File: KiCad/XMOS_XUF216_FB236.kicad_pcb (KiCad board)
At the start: 4 copper layers, 100 x 100 mm, 219 parts, among them J1 RJ45_Shielded, J10 Conn_02x10_FEMALE_toNext, J11 Conn_01x04, J12 Conn_01x08, J13 RJ45_Shielded, J14 RJ45_Shielded, J15 Conn_02x08_Odd_Even, J16 RJ45_Shielded, J17 RJ45_Shielded, J18 RJ45_Shielded, J19 RJ45_Shielded, J2 Barrel_Jack_MountingPin, J3 Conn_01x04, J4 RJ45_Shielded, J5 USB_B_Mini, J6 Conn_02x08_Odd_Even, J7 Mini-DIN-8, J8 Conn_02x10_MALE_FROM_XTAG, J9 Mini-DIN-8, M1 RFM-0505S, SW1 RESET, SW2 BOOT, SW3 GP, U1 DS90LV049TMT, U10 TPD2E2U06, U11 NC7WZ17, U12 NC7SZ157, U13 Si8642BA-B-IU, U14 DS90LV049TMT, U15 DS90LV049TMT, U16 DS90LV049TMT, U17 DS90LV049TMT, U18 DS90LV049TMT, U19 Si8642BA-B-IU, U2 IC-RES-TPS3808, U20 DS90LV049TMT, U3 IC-REG-ST1S06, U4 IC-REG-ST1S06, U5 IC-LOGIC-BUF-NC7WZ04P6X, U6 LM2574HVM-5, U7 MIC5504-3.3YM5, U8 DS90LV049TMT, U9 XUF216-512-FB236, X1 ASV-24MHz

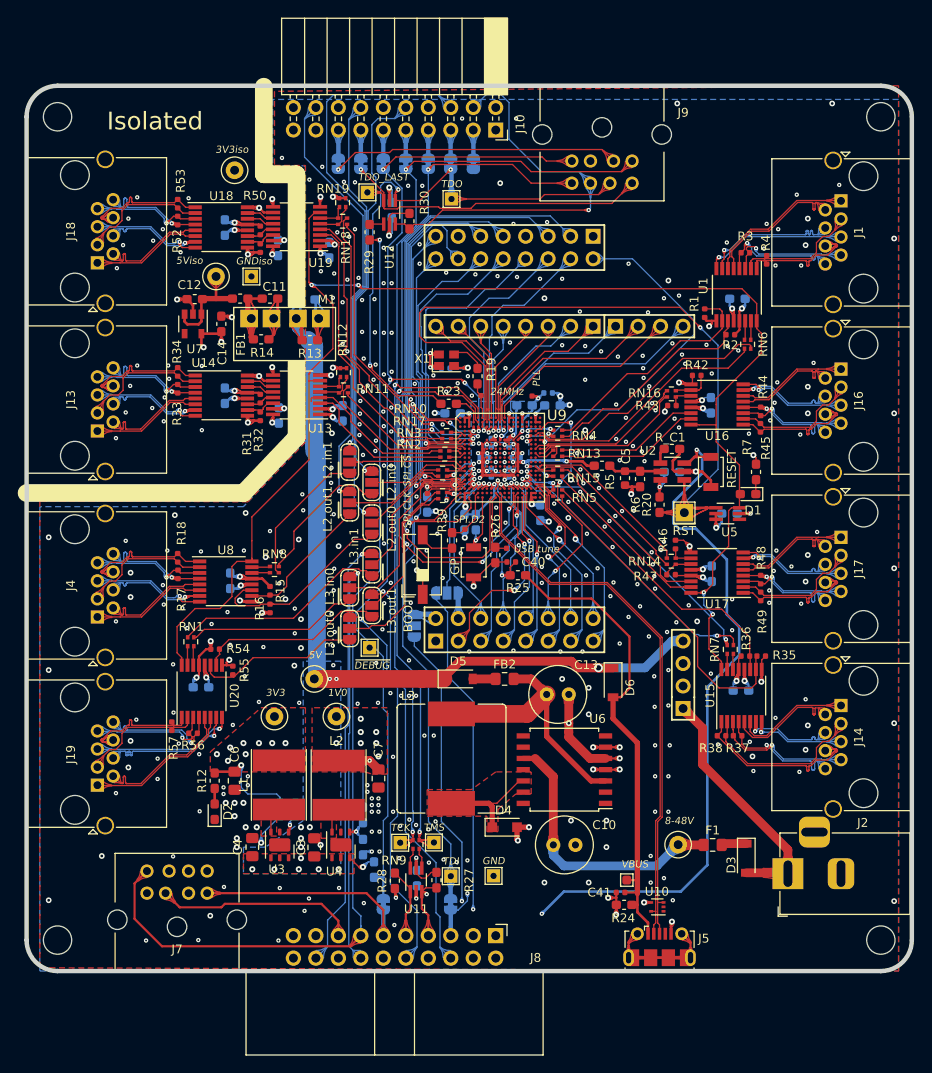
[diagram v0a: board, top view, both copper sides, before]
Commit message: Added impedance calc, and rerouted USB
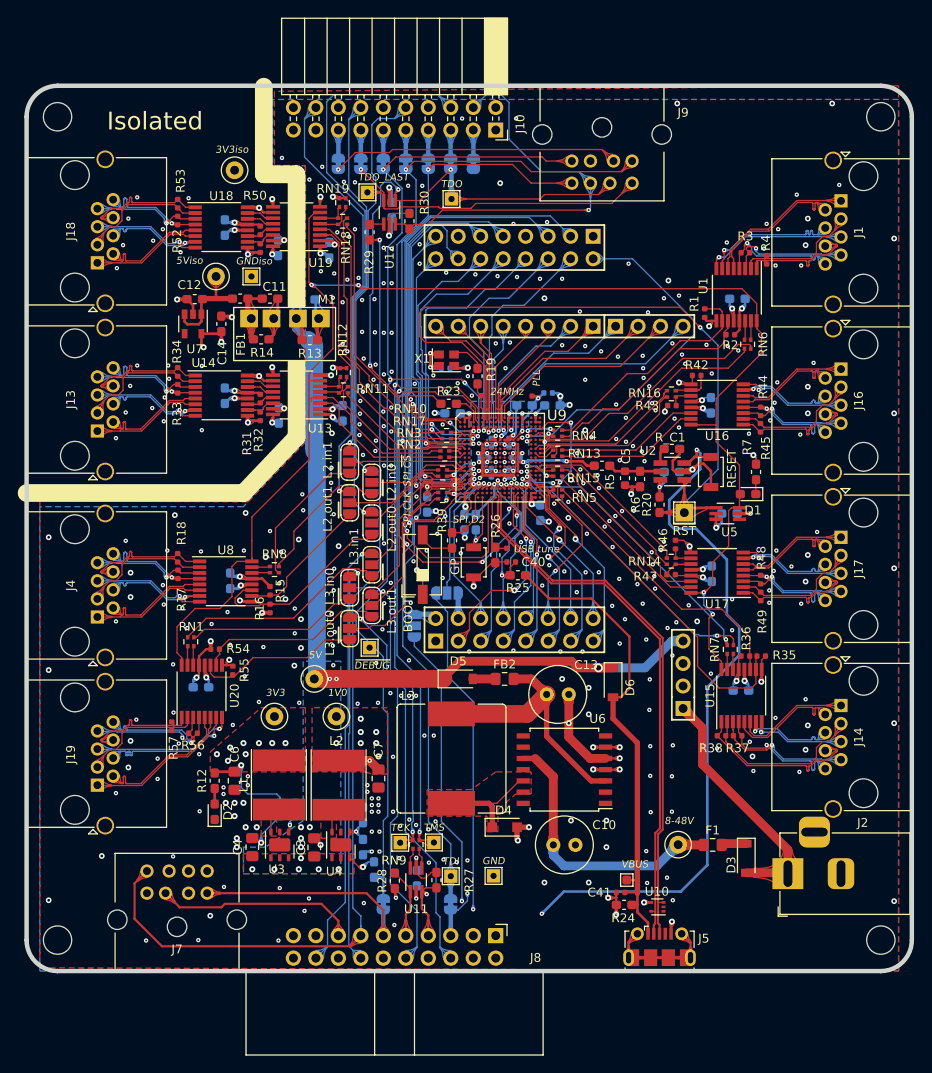
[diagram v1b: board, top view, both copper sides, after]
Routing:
- net GND: track 130.0 -> 131.0 mm, vias 426 -> 423
- net /~TRST: track 126.1 -> 126.6 mm
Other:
- net class LVDS added: clearance 0.0889, trace_width 0.0889, via_dia 0.4882, via_drill 0.2
- net class USB added: clearance 0.508, trace_width 0.0889, via_dia 0.4882, via_drill 0.2
- board text added: "LVDS needs to be redone to get 100R Zdiff impedance."
